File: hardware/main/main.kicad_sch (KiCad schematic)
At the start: 11 parts, among them J101 ST_LINK, J102 USART

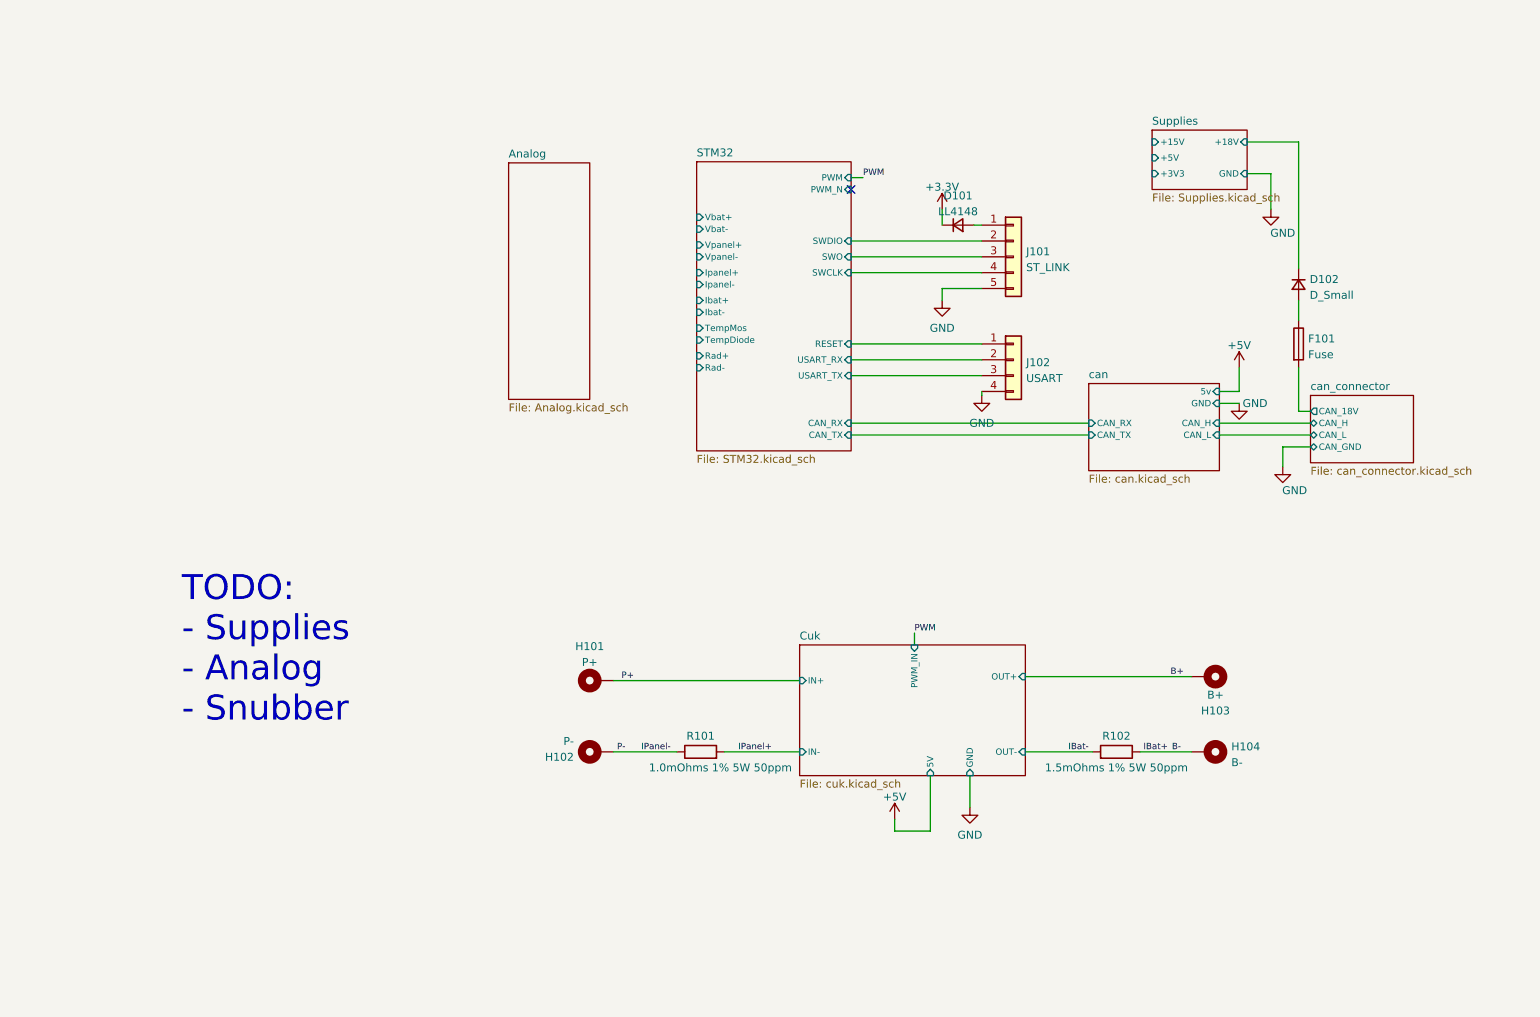
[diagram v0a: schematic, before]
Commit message: Schematics: finalize Analog Snubber and Supplies
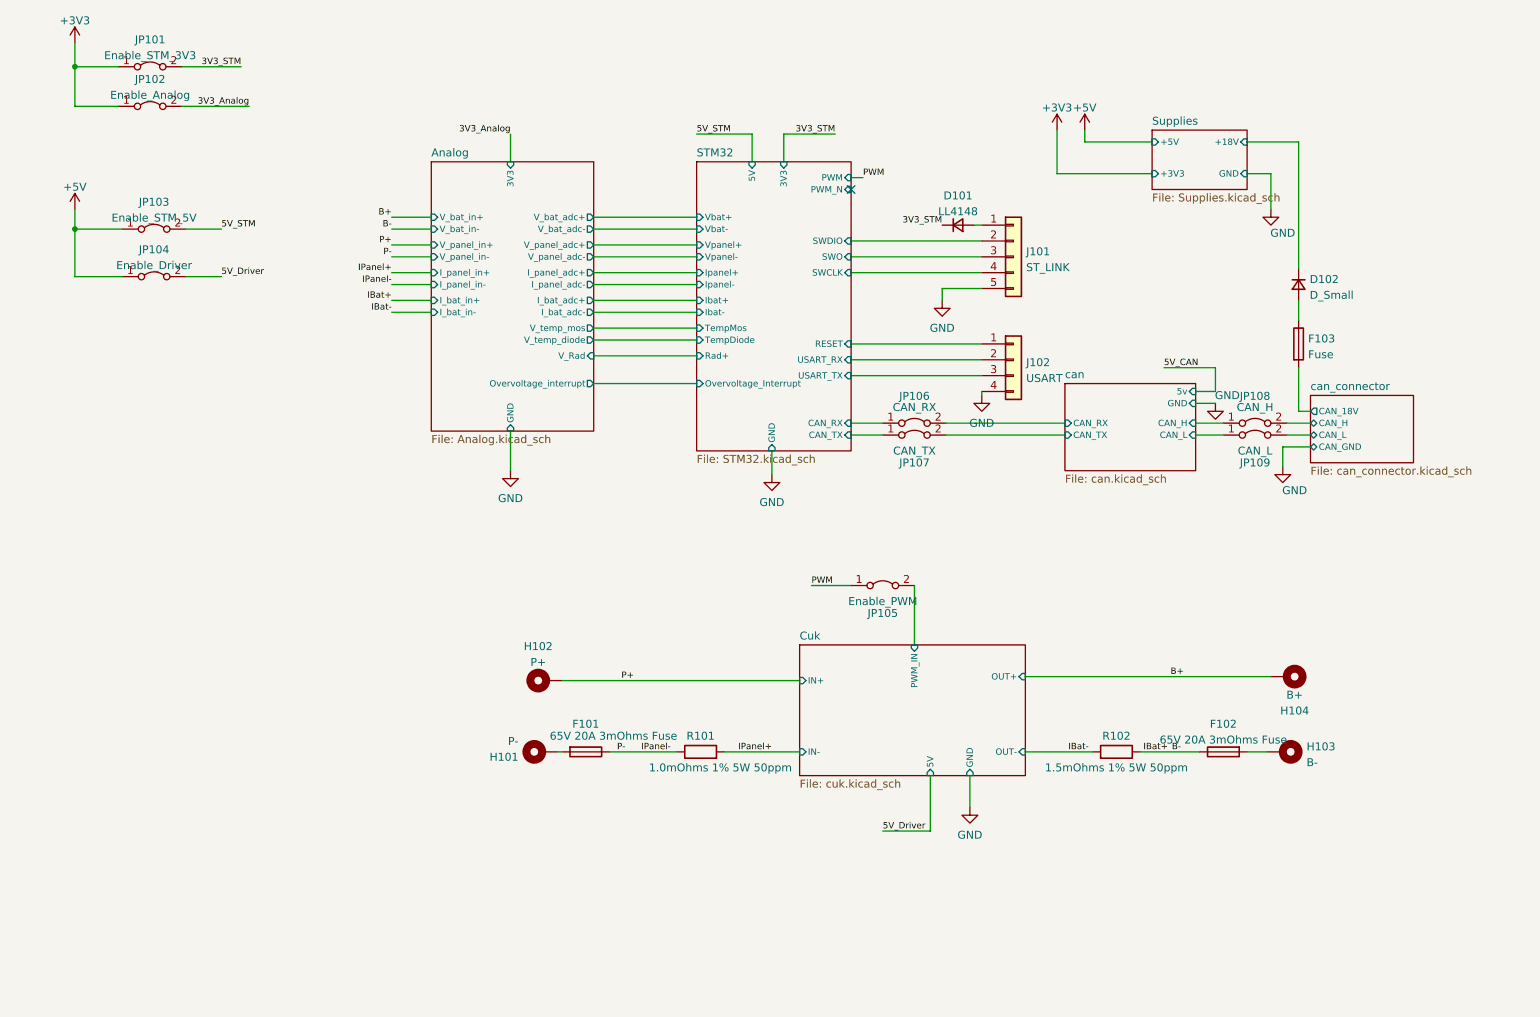
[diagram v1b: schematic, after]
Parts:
- added F101, F102: 65V 20A 3mOhms Fuse, symbol Device:Fuse
- added JP101: Enable_STM_3V3, symbol Jumper:Jumper_2_Bridged
- added JP102: Enable_Analog, symbol Jumper:Jumper_2_Bridged
- added JP103: Enable_STM_5V, symbol Jumper:Jumper_2_Bridged
- added JP104: Enable_Driver, symbol Jumper:Jumper_2_Bridged
- added JP105: Enable_PWM, symbol Jumper:Jumper_2_Bridged
- added JP106: CAN_RX, symbol Jumper:Jumper_2_Bridged
- added JP107: CAN_TX, symbol Jumper:Jumper_2_Bridged
- added JP108: CAN_H, symbol Jumper:Jumper_2_Bridged
- added JP109: CAN_L, symbol Jumper:Jumper_2_Bridged
- renumbered F101 to F103, H102 to H101, H101 to H102, H104 to H103, H103 to H104
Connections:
- net +5V: now also JP103.1 (A), JP104.1 (A)
- net B-: now also F102.1; no longer H103.1
- net IPanel-: now also F101.1; no longer H101.1
- net PWM: now also JP105.1 (A)
- net STM32/CAN_RX: now also JP106.1 (A)
- net STM32/CAN_TX: now also JP107.1 (A)
- net can/CAN_H: now also JP108.1 (A)
- net can/CAN_L: now also JP109.1 (A)
- net +3.3V renamed 3V3_STM
- net 3V3_STM: now also JP101.2 (B)
- new net: F102.2, H103.1
- new net: F101.2, H101.1
- new net +3V3: JP101.1 (A), JP102.1 (A)
- new net 3V3_Analog: JP102.2 (B)
- new net 5V_Driver: JP104.2 (B)
- new net 5V_STM: JP103.2 (B)
- new net Cuk/PWM_IN: JP105.2 (B)
- new net can/CAN_RX: JP106.2 (B)
- new net can/CAN_TX: JP107.2 (B)
- new net can_connector/CAN_H: JP108.2 (B)
- new net can_connector/CAN_L: JP109.2 (B)
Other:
- sheet Analog ports: added 3V3, GND, I_bat_adc+, I_bat_adc-, I_bat_in+, I_bat_in-, I_panel_adc+, I_panel_adc-, I_panel_in+, I_panel_in-, Overvoltage_interrupt, V_Rad, V_bat_adc+, V_bat_adc-, V_bat_in+, V_bat_in-, V_panel_adc+, V_panel_adc-, V_panel_in+, V_panel_in-, V_temp_diode, V_temp_mos; removed none
- sheet STM32 ports: added 3V3, 5V, GND, Overvoltage_Interrupt; removed Rad-
- sheet Supplies ports: added none; removed +15V
- note removed: "TODO: - Supplies - Analog - Snubber"
- moved on the sheet: H101, H102, H103, H104

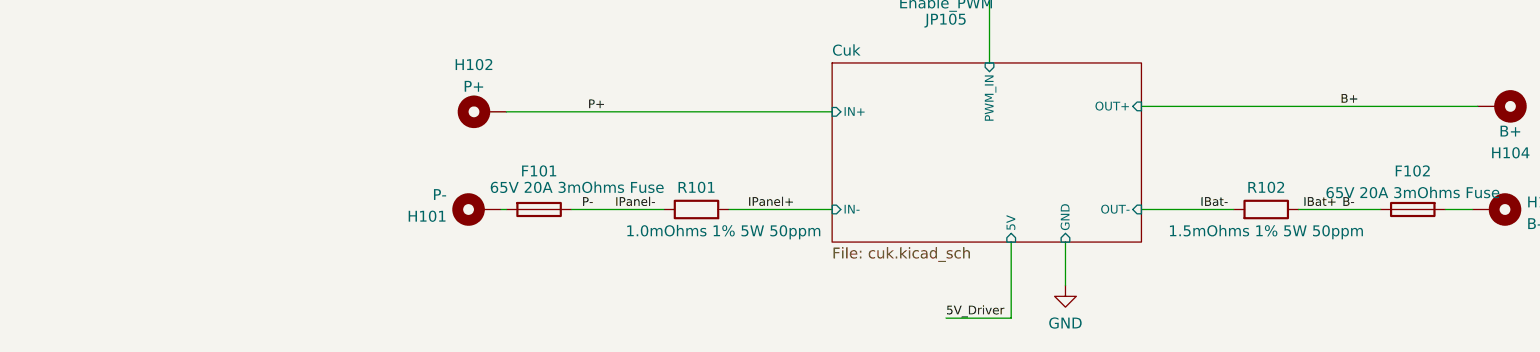
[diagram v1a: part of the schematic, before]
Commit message: Schematics: Modified component values
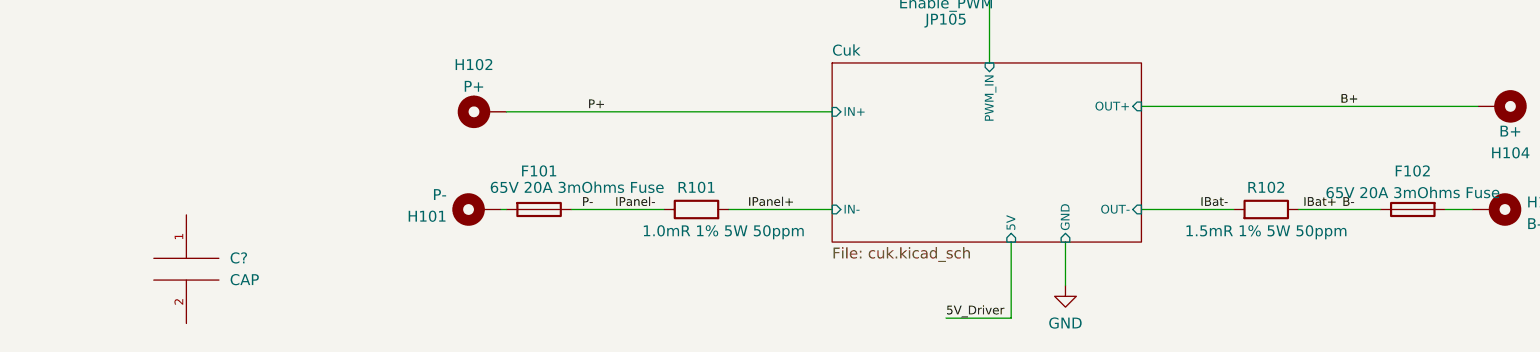
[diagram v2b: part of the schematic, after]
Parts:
- added C?: CAP, symbol pspice:CAP
- R101: value 1.0mOhms 1% 5W 50ppm -> 1.0mR 1% 5W 50ppm
- R102: value 1.5mOhms 1% 5W 50ppm -> 1.5mR 1% 5W 50ppm

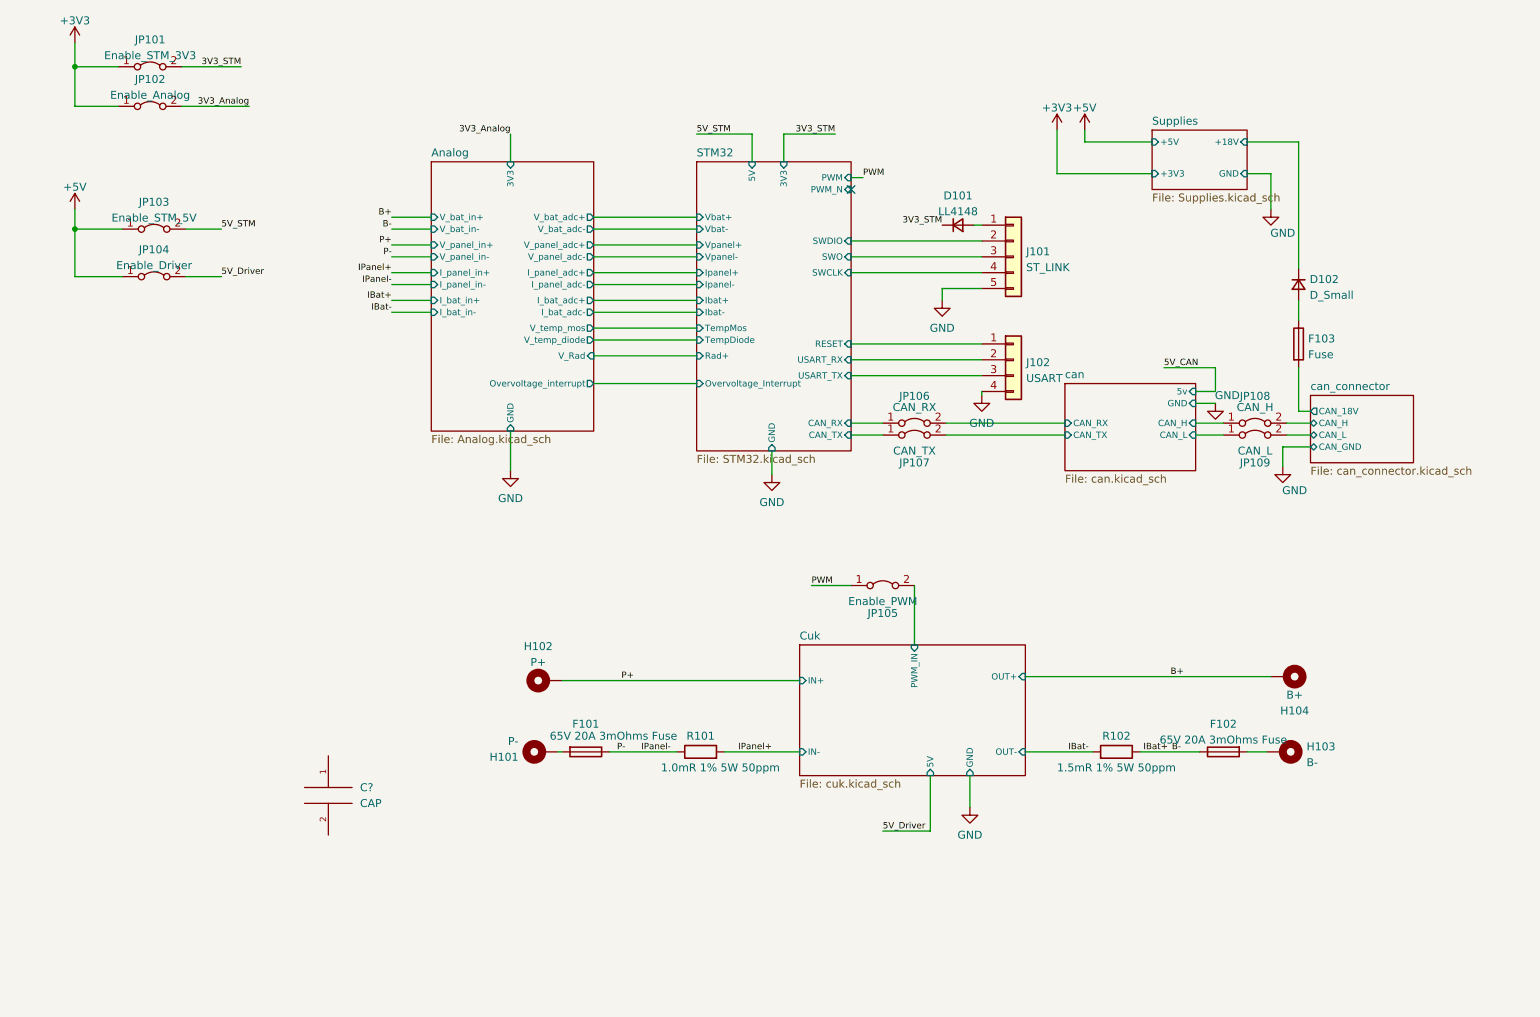
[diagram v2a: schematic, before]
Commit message: Schematics: Sym table and libs updated
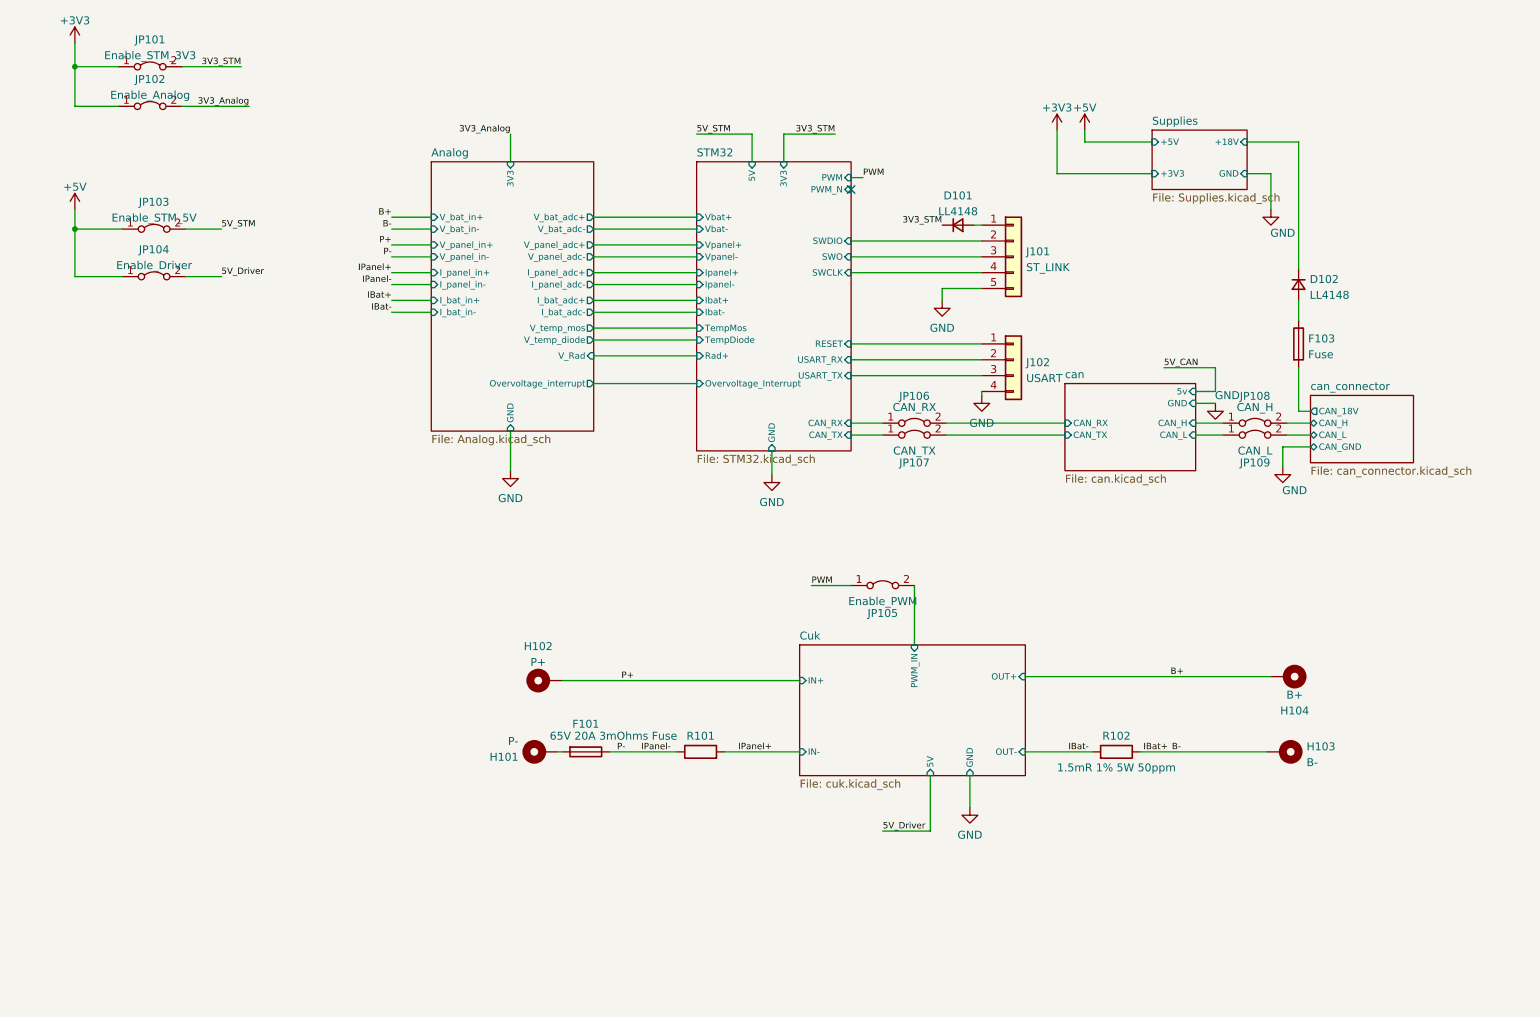
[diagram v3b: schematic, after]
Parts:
- removed C?: CAP, symbol pspice:CAP
- removed F102: 65V 20A 3mOhms Fuse, symbol Device:Fuse
- D102: value D_Small -> LL4148
- R101: value 1.0mR 1% 5W 50ppm -> (none)
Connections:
- net B-: now also H103.1

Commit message: Schematics: Run DRC and fix errors and some warnings, also added Zenite kicad library repo as submodule
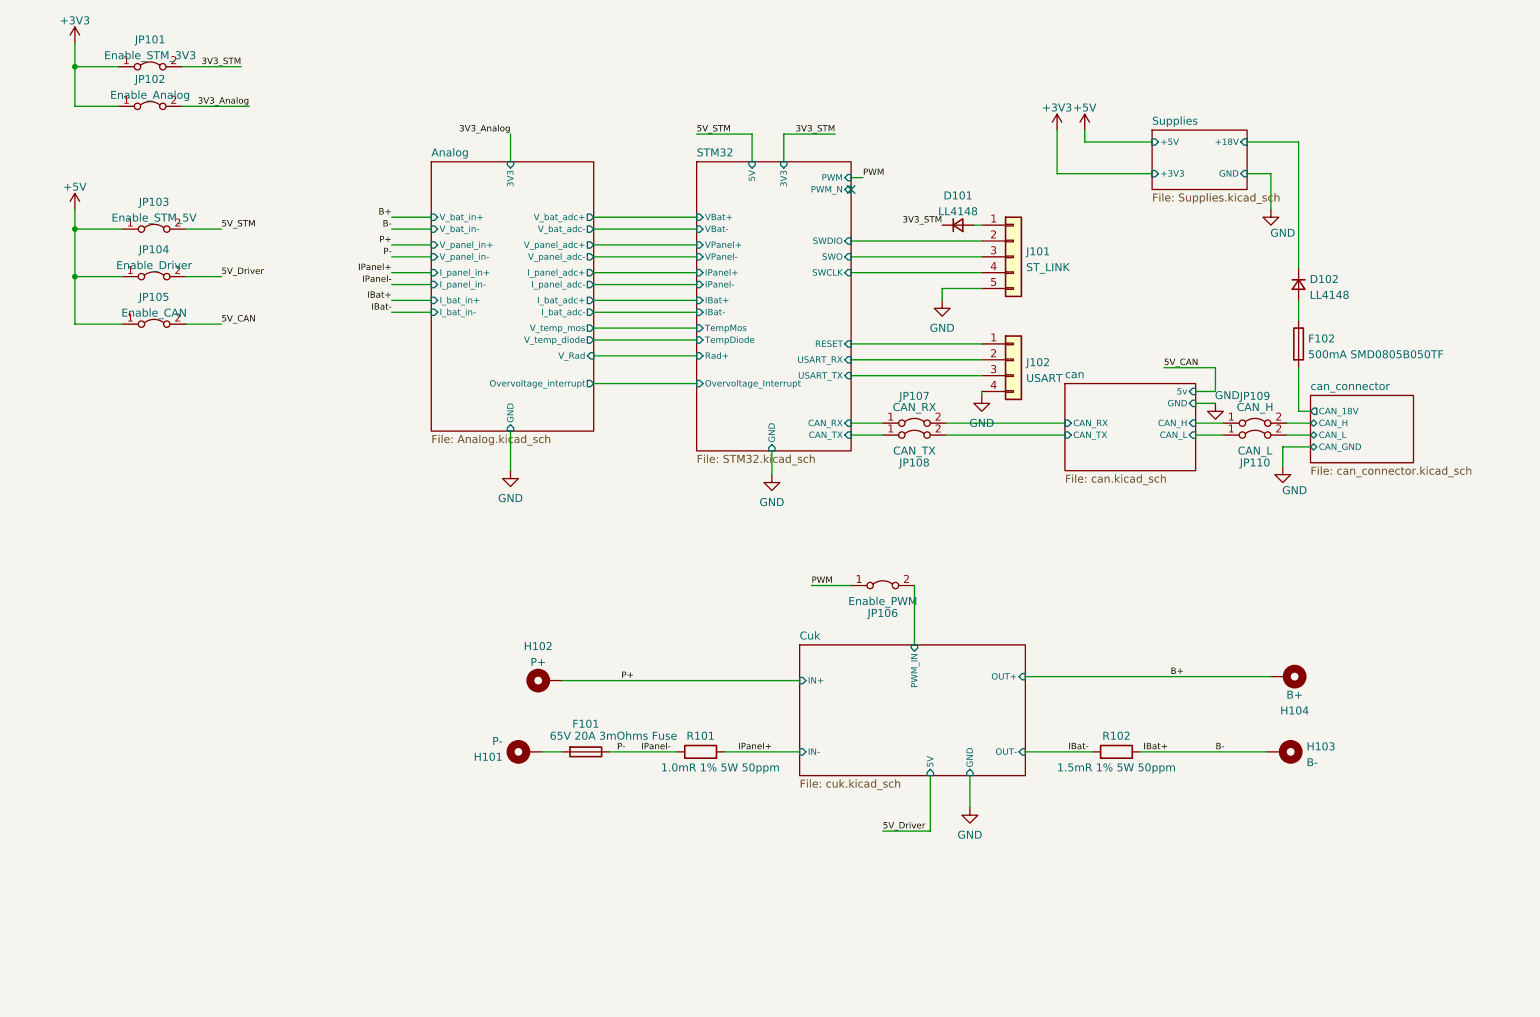
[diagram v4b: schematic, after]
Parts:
- added JP105: Enable_CAN, Jumper:SolderJumper-2_P1.3mm_Open_TrianglePad1.0x1.5mm, symbol Jumper:Jumper_2_Bridged
- D101, D102: footprint (none) -> Diode_SMD:D_MiniMELF_Handsoldering
- F101: footprint (none) -> Zenite:S6125-F
- F102: renamed from F103; value Fuse -> 500mA SMD0805B050TF; footprint (none) -> Fuse:Fuse_0805_2012Metric_Pad1.15x1.40mm_HandSolder
- H101, H102, H103, H104: footprint (none) -> Zenite:MountingHole_12mmx12mm_Rectangular
- J101: footprint (none) -> Zenite:PinSocket_1x05_P2.54mm_Horizontal_SMD
- J102: footprint (none) -> Zenite:PinSocket_1x04_P2.54mm_Horizontal_SMD
- JP101, JP102, JP103, JP104: footprint (none) -> Jumper:SolderJumper-2_P1.3mm_Open_TrianglePad1.0x1.5mm
- JP106: renamed from JP105; footprint (none) -> Jumper:SolderJumper-2_P1.3mm_Open_TrianglePad1.0x1.5mm
- JP107: renamed from JP106; footprint (none) -> Jumper:SolderJumper-2_P1.3mm_Open_TrianglePad1.0x1.5mm
- JP108: renamed from JP107; footprint (none) -> Jumper:SolderJumper-2_P1.3mm_Open_TrianglePad1.0x1.5mm
- JP109: renamed from JP108; footprint (none) -> Jumper:SolderJumper-2_P1.3mm_Open_TrianglePad1.0x1.5mm
- JP110: renamed from JP109; footprint (none) -> Jumper:SolderJumper-2_P1.3mm_Open_TrianglePad1.0x1.5mm
- R101: value (none) -> 1.0mR 1% 5W 50ppm; footprint (none) -> Resistor_SMD:R_2512_6332Metric_Pad1.40x3.35mm_HandSolder
- R102: footprint (none) -> Resistor_SMD:R_2512_6332Metric_Pad1.40x3.35mm_HandSolder
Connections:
- net +5V: now also JP105.1 (A)
- net 5V_CAN: now also JP105.2 (B)
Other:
- sheet STM32 ports: added IBat+, IBat-, IPanel+, IPanel-, VBat+, VBat-, VPanel+, VPanel-; removed Ibat+, Ibat-, Ipanel+, Ipanel-, Vbat+, Vbat-, Vpanel+, Vpanel-
- moved on the sheet: H101
